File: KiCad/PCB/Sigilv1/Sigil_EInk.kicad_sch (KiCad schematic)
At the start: 6 parts, among them J2 INLAND E-PAPER HEADER (8-PIN), J3 BUZZER LOGICAL ONLY, J4 ANALOG JOYSTICK HEADER (5-PIN), J5 NEOPIXEL JEWEL 7 RGBW, U1 REMOVABLE ESP32 DEVKIT / 2 x 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

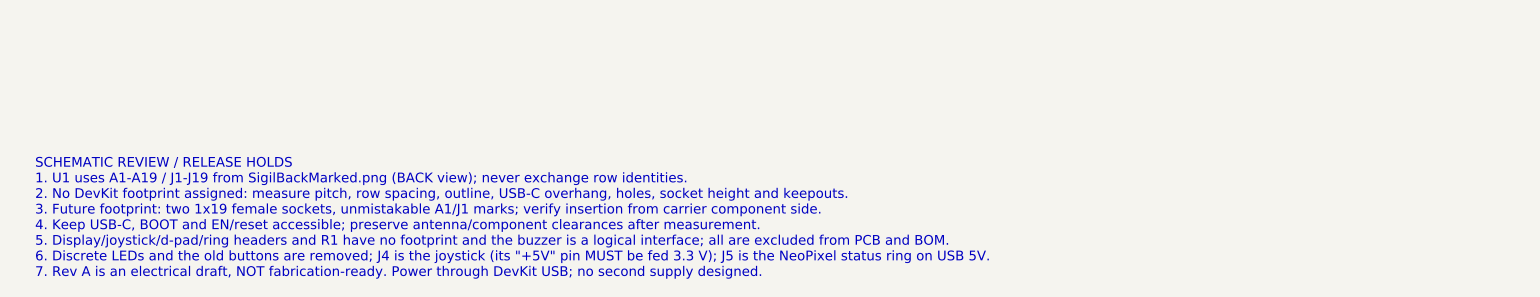
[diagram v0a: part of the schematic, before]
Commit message: OLED Sigil schematic: five discrete pushbuttons replace the d-pad header
J4 (a d-pad module header) becomes SW1-SW5, momentary pushbuttons from
each key GPIO to a shared GND with the internal pull-ups: Up J11/GPIO25,
Down J9/GPIO27, Left A12/GPIO19, Right A14/GPIO21, Select J13/GPIO32.
Firmware already reads them this way. Rebuilt with build_schematic.py;
verify_schematic.py passes and KiCad ERC reports 0 violations on both
schematics.

Co-Authored-By: Claude Opus 5.5 <noreply@anthropic.com>
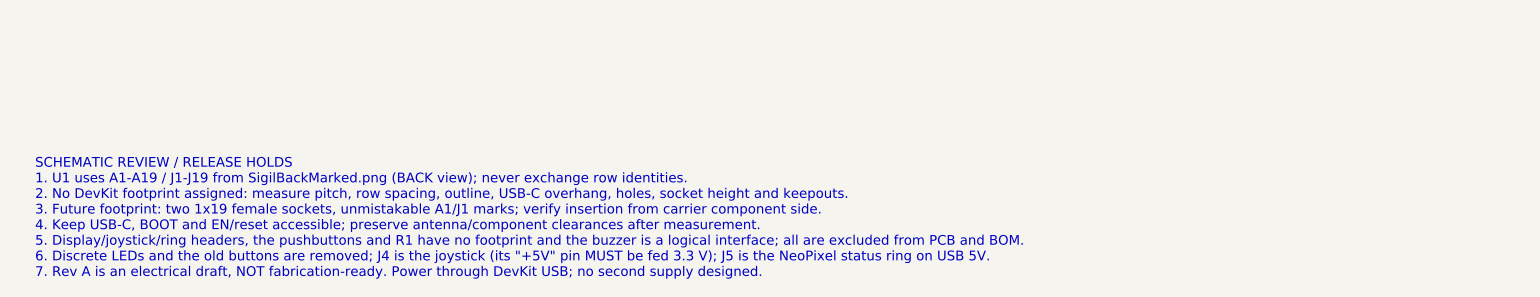
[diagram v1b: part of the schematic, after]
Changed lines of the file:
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@@
-		)
-	)
-	(text "SCHEMATIC REVIEW / RELEASE HOLDS\n1. U1 uses A1-A19 / J1-J19 from SigilBackMarked.png (BACK view); never exchange row identities.\n2. No DevKit footprint assigned: measure pitch, row spacing, outline, USB-C overhang, holes, socket height and keepouts.\n3. Future footprint: two 1x19 female sockets, unmistakable A1/J1 marks; verify insertion from carrier component side.\n4. Keep USB-C, BOOT and EN/reset accessible; preserve antenna/component clearances after measurement.\n5. Display/joystick/d-pad/ring headers and R1 have no footprint and the buzzer is a logical interface; all are excluded from PCB and BOM.\n6. Discrete LEDs and the old buttons are removed; J4 is the joystick (its \"+5V\" pin MUST be fed 3.3 V); J5 is the NeoPixel status ring on USB 5V.\n7. Rev A is an electrical draft, NOT fabrication-ready. Power through DevKit USB; no second supply designed."
-		(exclude_from_sim no)
-		(at 28 211 0)
-		(effects
-			(font
-				(size 1.27 1.27)
-			)
-			(justify left top)
 		)
 	)
@@
 			)
 			(justify left top)
+		)
+	)
+	(text "SCHEMATIC REVIEW / RELEASE HOLDS\n1. U1 uses A1-A19 / J1-J19 from SigilBackMarked.png (BACK view); never exchange row identities.\n2. No DevKit footprint assigned: measure pitch, row spacing, outline, USB-C overhang, holes, socket height and keepouts.\n3. Future footprint: two 1x19 female sockets, unmistakable A1/J1 marks; verify insertion from carrier component side.\n4. Keep USB-C, BOOT and EN/reset accessible; preserve antenna/component clearances after measurement.\n5. Display/joystick/ring headers, the pushbuttons and R1 have no footprint and the buzzer is a logical interface; all are excluded from PCB and BOM.\n6. Discrete LEDs and the old buttons are removed; J4 is the joystick (its \"+5V\" pin MUST be fed 3.3 V); J5 is the NeoPixel status ring on USB 5V.\n7. Rev A is an electrical draft, NOT fabrication-ready. Power through DevKit USB; no second supply designed."
+		(exclude_from_sim no)
+		(at 28 211 0)
+		(effects
+			(font
+				(size 1.27 1.27)
+			)
+			(justify left top)

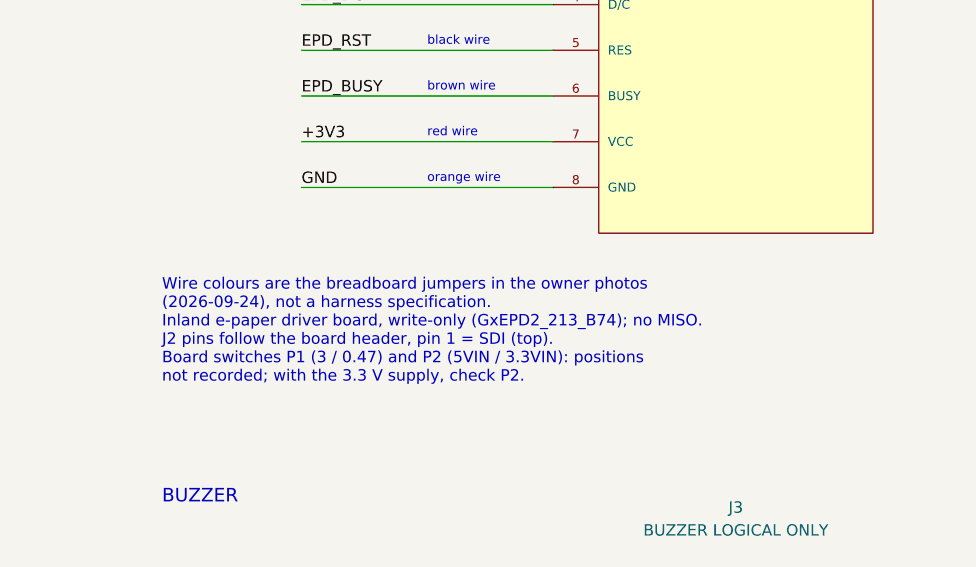
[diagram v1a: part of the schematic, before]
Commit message: Turntest notes: softer white, OLED key help, pass countdown, living heart, US spellings
- Jewel: full RGB white (hold fill, starter, lobby invite) is now a soft
  warm white; it was glaring next to every other cue.
- OLED game screen: one line of key help under the life total
  ("<> life  press: menu", or "Click again to undo" while passing).
- Pending pass: Sigils show PASSING and a green ring countdown while
  Undo pass is on offer; a second Select on the OLED undoes the pass.
  Atlas's screen counts down "Passing in Ns". PASS_GRACE_MS moves to
  protocol.h so both firmwares share it; Atlas still owns the timer.
- Life heart: new StartingLife packet (37, Atlas -> menu Sigils, resent
  with Hello; older Sigils ignore it). The heart drains from the top below
  the starting life and grows up to 1.5x at double it.
- US spellings in UI text, comments, docs, KiCad notes and manual V0.3.
  Wire tokens (CANCELLED) and code identifiers are unchanged.

Co-Authored-By: Claude Opus 5.5 <noreply@anthropic.com>
Claude-Session: https://claude.ai/code/session_019MjMMnFUjQwKLv4TjtKLwb
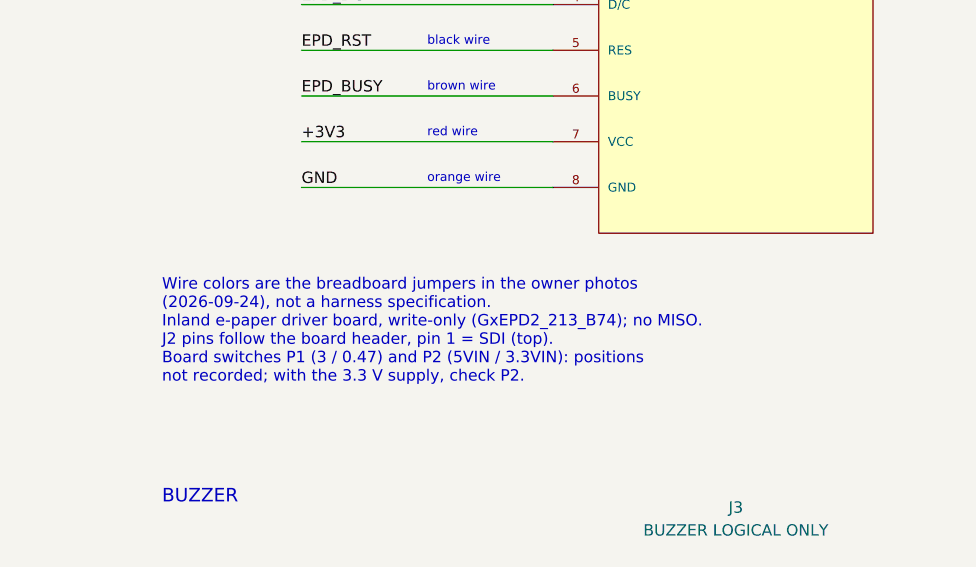
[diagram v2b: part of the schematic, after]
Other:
- note added: "Wire colors are the breadboard jumpers in the owner photos (2026-09-24), not a harness specification. Inland e-paper driver board, write-only (GxEPD2_213_B74); no MISO. J2 pins follow the board header, pin 1 = SDI (top). Board switches P1 (3 / 0.47) and P2 (5VIN / 3.3VIN): positions not recorded; with the 3.3 V supply, check P2."
- note removed: "Wire colours are the breadboard jumpers in the owner photos (2026-09-24), not a harness specification. Inland e-paper driver board, write-only (GxEPD2_213_B74); no MISO. J2 pins follow the board header, pin 1 = SDI (top). Board switches P1 (3 / 0.47) and P2 (5VIN / 3.3VIN): positions not recorded; with the 3.3 V supply, check P2."
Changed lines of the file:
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@@
 		)
 	)
-	(text "Wire colours are the breadboard jumpers in the owner photos\n(2026-09-24), not a harness specification.\nInland e-paper driver board, write-only (GxEPD2_213_B74); no MISO.\nJ2 pins follow the board header, pin 1 = SDI (top).\nBoard switches P1 (3 / 0.47) and P2 (5VIN / 3.3VIN): positions\nnot recorded; with the 3.3 V supply, check P2."
+	(text "Wire colors are the breadboard jumpers in the owner photos\n(2026-09-24), not a harness specification.\nInland e-paper driver board, write-only (GxEPD2_213_B74); no MISO.\nJ2 pins follow the board header, pin 1 = SDI (top).\nBoard switches P1 (3 / 0.47) and P2 (5VIN / 3.3VIN): positions\nnot recorded; with the 3.3 V supply, check P2."
 		(exclude_from_sim no)
 		(at 175 101.6 0)

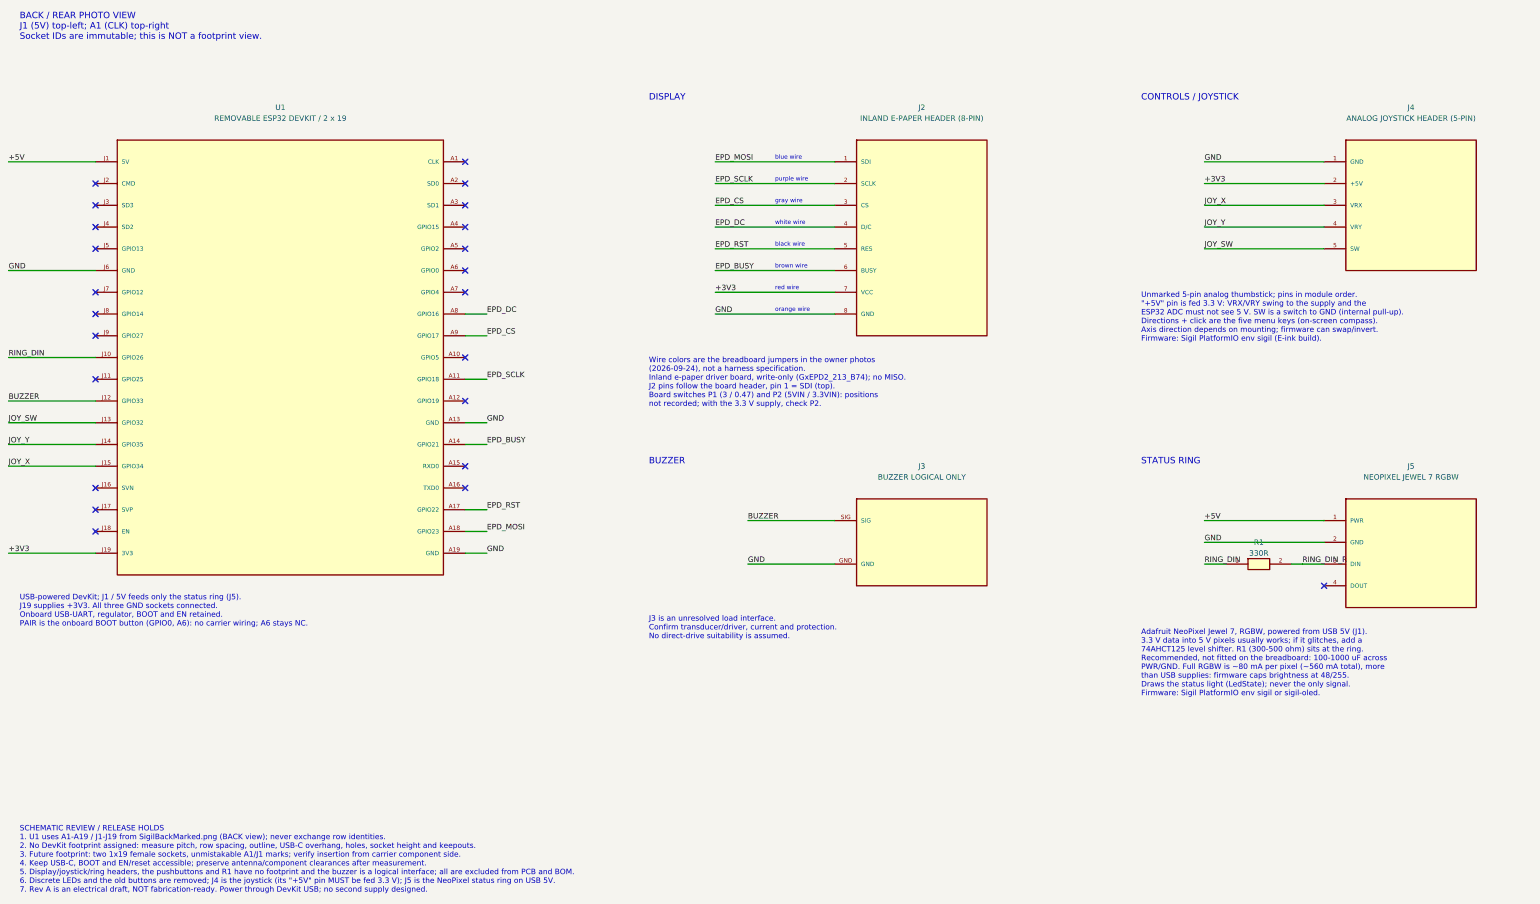
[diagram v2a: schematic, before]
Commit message: Sigil schematics: first-PCB footprints, GPIO4 display strap, ring and 3V3 capacitors
- Every carrier part except the DevKit (U1) gets a through-hole footprint
  and joins the BOM; J3 becomes a numbered 2-pin buzzer header.
- A7/GPIO4 strap: open on the E-ink board, GND on the OLED board, matching
  HW_TYPE_STRAP_PIN (the OLED draft had it NC, which would halt at boot).
- C1 470 uF across the Jewel supply, C2 10 uF on +3V3.
- tools/offline_netlist.py lets verify_schematic.py run without KiCad;
  ERC still needs a KiCad re-run.

Co-Authored-By: Claude Opus 5.5 <noreply@anthropic.com>
Claude-Session: https://claude.ai/code/session_01EuTMd98XaCZ1DRqGGQFyaV
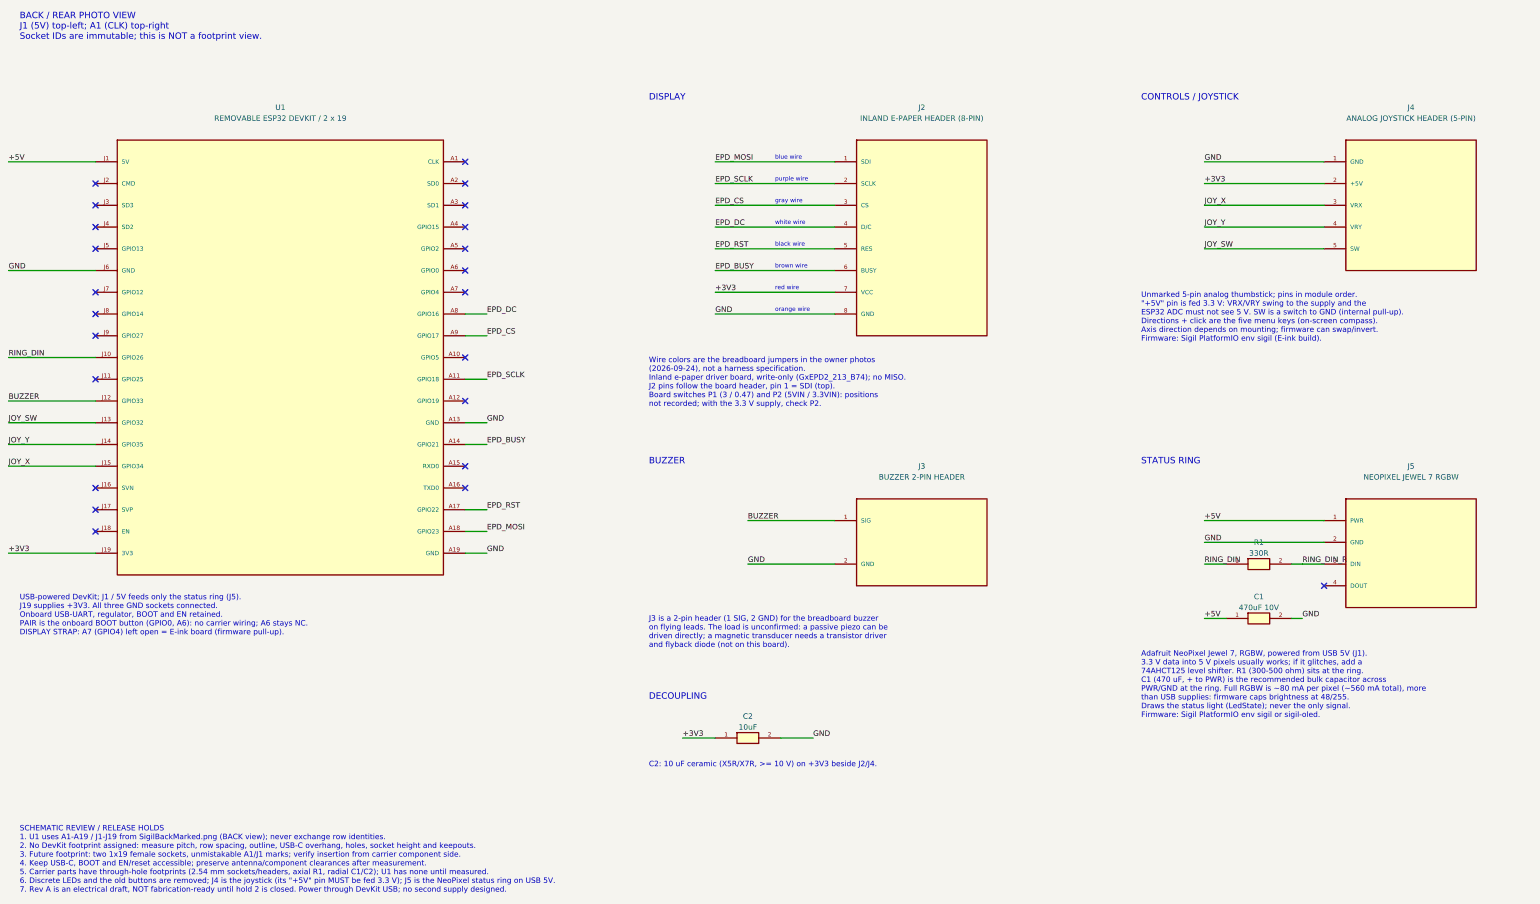
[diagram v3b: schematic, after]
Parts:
- added C1: 470uF 10V, Capacitor_THT:CP_Radial_D8.0mm_P3.50mm, symbol Sigil:Capacitor
- added C2: 10uF, Capacitor_THT:C_Disc_D5.0mm_W2.5mm_P5.00mm, symbol Sigil:Capacitor
- J2: footprint (none) -> Connector_PinSocket_2.54mm:PinSocket_1x08_P2.54mm_Vertical; now in the parts list
- J3: value BUZZER LOGICAL ONLY -> BUZZER 2-PIN HEADER; footprint (none) -> Connector_PinHeader_2.54mm:PinHeader_1x02_P2.54mm_Vertical; now in the parts list
- J4: footprint (none) -> Connector_PinSocket_2.54mm:PinSocket_1x05_P2.54mm_Vertical; now in the parts list
- J5: footprint (none) -> Connector_PinHeader_2.54mm:PinHeader_1x04_P2.54mm_Vertical; now in the parts list
- R1: footprint (none) -> Resistor_THT:R_Axial_DIN0207_L6.3mm_D2.5mm_P7.62mm_Horizontal; now in the parts list
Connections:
- net +3V3: now also C2.1
- net +5V: now also C1.1
- net BUZZER: now also J3.1 (SIG); no longer J3.SIG
- net GND: now also J3.2 (GND), C1.2, C2.2; no longer J3.GND
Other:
- note added: "Adafruit NeoPixel Jewel 7, RGBW, powered from USB 5V (J1). 3.3 V data into 5 V pixels usually works; if it glitches, add a 74AHCT125 level shifter. R1 (300-500 ohm) sits at the ring. C1 (470 uF, + to PWR) is the recommended bulk capacitor across PWR/GND at the ring. Full RGBW is ~80 mA per pixel (~560 mA total), more than USB supplies: firmware caps brightness at 48/255. Draws the status light (L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"
- note added: "C2: 10 uF ceramic (X5R/X7R, >= 10 V) on +3V3 beside J2/J4."
- note added: "DECOUPLING"
- note added: "J3 is a 2-pin header (1 SIG, 2 GND) for the breadboard buzzer on flying leads. The load is unconfirmed: a passive piezo can be driven directly; a magnetic transducer needs a transistor driver and flyback diode (not on this board)."
- note added: "USB-powered DevKit; J1 / 5V feeds only the status ring (J5). J19 supplies +3V3. All three GND sockets connected. Onboard USB-UART, regulator, BOOT and EN retained. PAIR is the onboard BOOT button (GPIO0, A6): no carrier wiring; A6 stays NC. DISPLAY STRAP: A7 (GPIO4) left open = E-ink board (firmware pull-up)."
- note removed: "Adafruit NeoPixel Jewel 7, RGBW, powered from USB 5V (J1). 3.3 V data into 5 V pixels usually works; if it glitches, add a 74AHCT125 level shifter. R1 (300-500 ohm) sits at the ring. Recommended, not fitted on the breadboard: 100-1000 uF across PWR/GND. Full RGBW is ~80 mA per pixel (~560 mA total), more than USB supplies: firmware caps brightness at 48/255. Draws the status light (LedState); nev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"
- note removed: "J3 is an unresolved load interface. Confirm transducer/driver, current and protection. No direct-drive suitability is assumed."
- note removed: "USB-powered DevKit; J1 / 5V feeds only the status ring (J5). J19 supplies +3V3. All three GND sockets connected. Onboard USB-UART, regulator, BOOT and EN retained. PAIR is the onboard BOOT button (GPIO0, A6): no carrier wiring; A6 stays NC."
